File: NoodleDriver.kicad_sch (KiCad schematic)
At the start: 21 parts, among them J1 Conn_01x04, J2 Conn_01x04, J6 Conn_01x04, J7 Conn_01x04, J8 Conn_01x08, U1 WS2811, U2 WS2811, U3 ULN2001, U4 74HC04

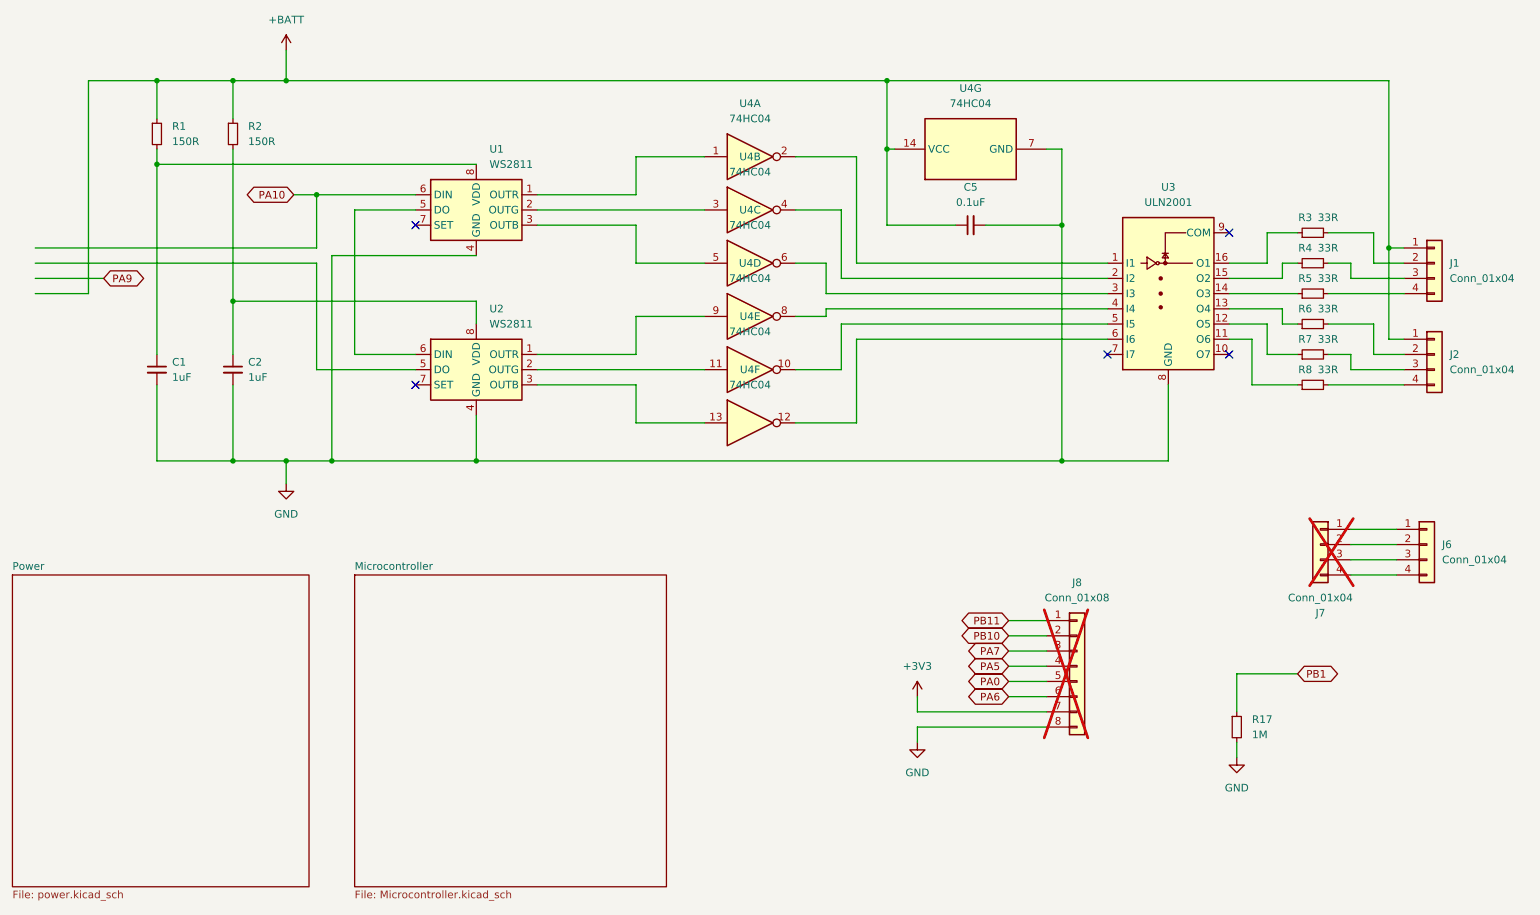
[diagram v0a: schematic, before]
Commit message: Fix footprint bugs (and remove WS2811 interfaces).  Part of #5
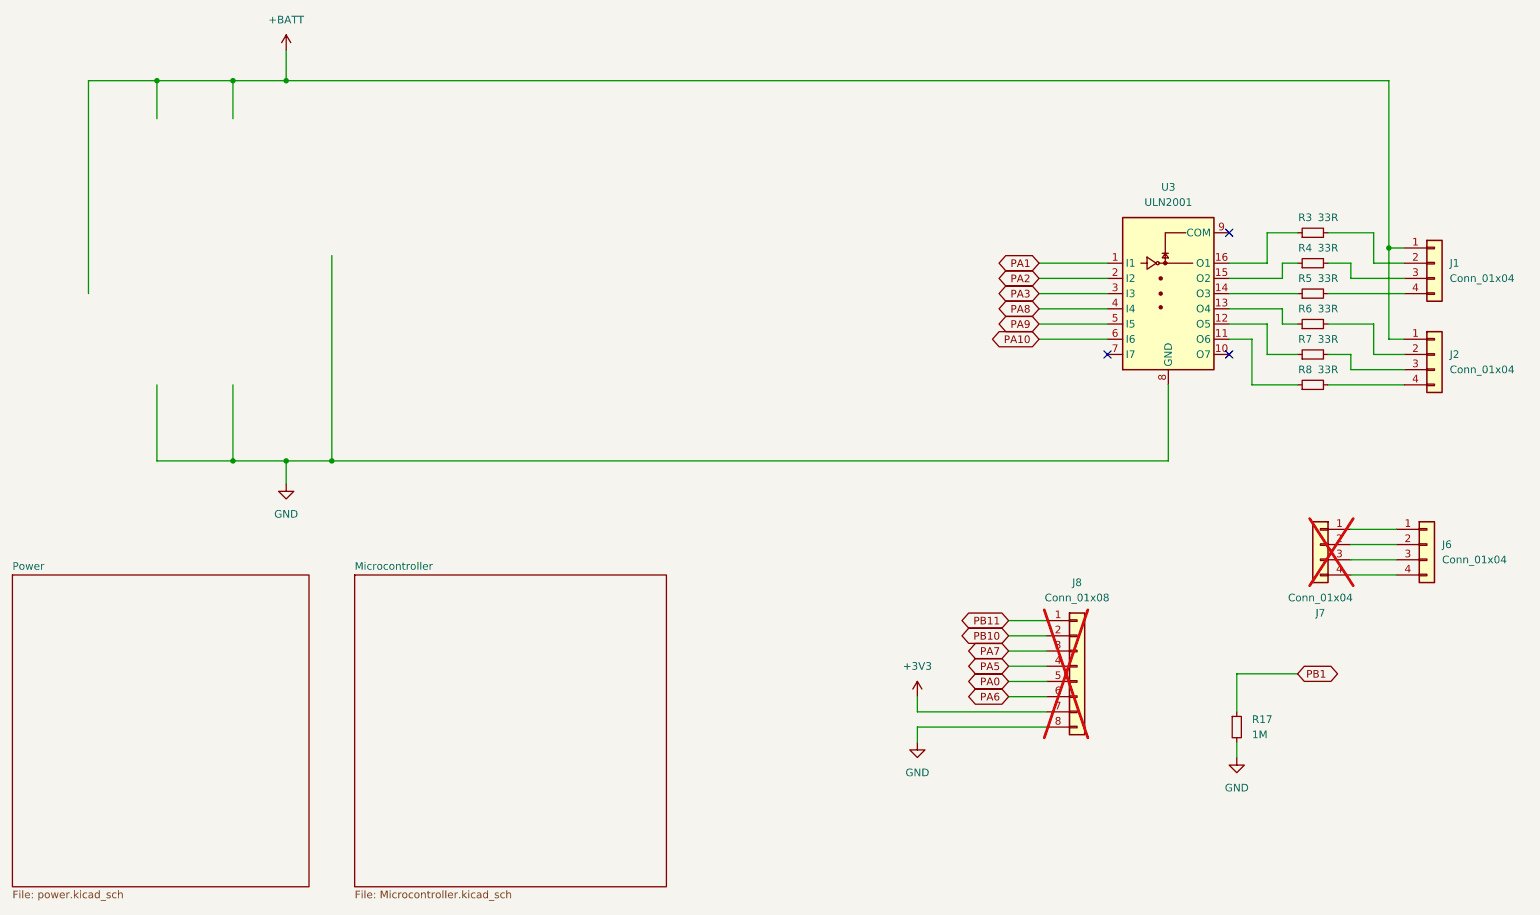
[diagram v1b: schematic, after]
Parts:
- removed C1, C2: 1uF, Capacitor_SMD:C_0402_1005Metric, symbol Device:C_Small
- removed C5: 0.1uF, Capacitor_SMD:C_0402_1005Metric, symbol Device:C_Small
- removed R1, R2: 150R, Resistor_SMD:R_0402_1005Metric, symbol Device:R_Small
- removed U1, U2: WS2811, Package_SO:SOP-8_3.76x4.96mm_P1.27mm, symbol Driver_LED:WS2811
- removed U4: 74HC04, Package_SO:SOIC-14_3.9x8.7mm_P1.27mm, symbol 74xx:74HC04
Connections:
- net PA10: now also U3.6 (I6)
- net PA9: now also U3.5 (I5)
- net PA8: now reaches U3.4 (I4)
- net PA1: now reaches U3.1 (I1)
- net PA2: now reaches U3.2 (I2)
- net PA3: now reaches U3.3 (I3)
- no-connect marks 5 -> 3
